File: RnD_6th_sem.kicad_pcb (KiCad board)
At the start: 2 copper layers, 62.1 x 60.5 mm, 63 parts, among them IC1 2EDF7275KXUMA1, J1 HVDC1, J2 PWM, J3 HVDC2, J4 Conn_02x04_Odd_Even, J5 5V, J6 5V, J7 GND2, J8 GND1, J9 Conn_02x04_Odd_Even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

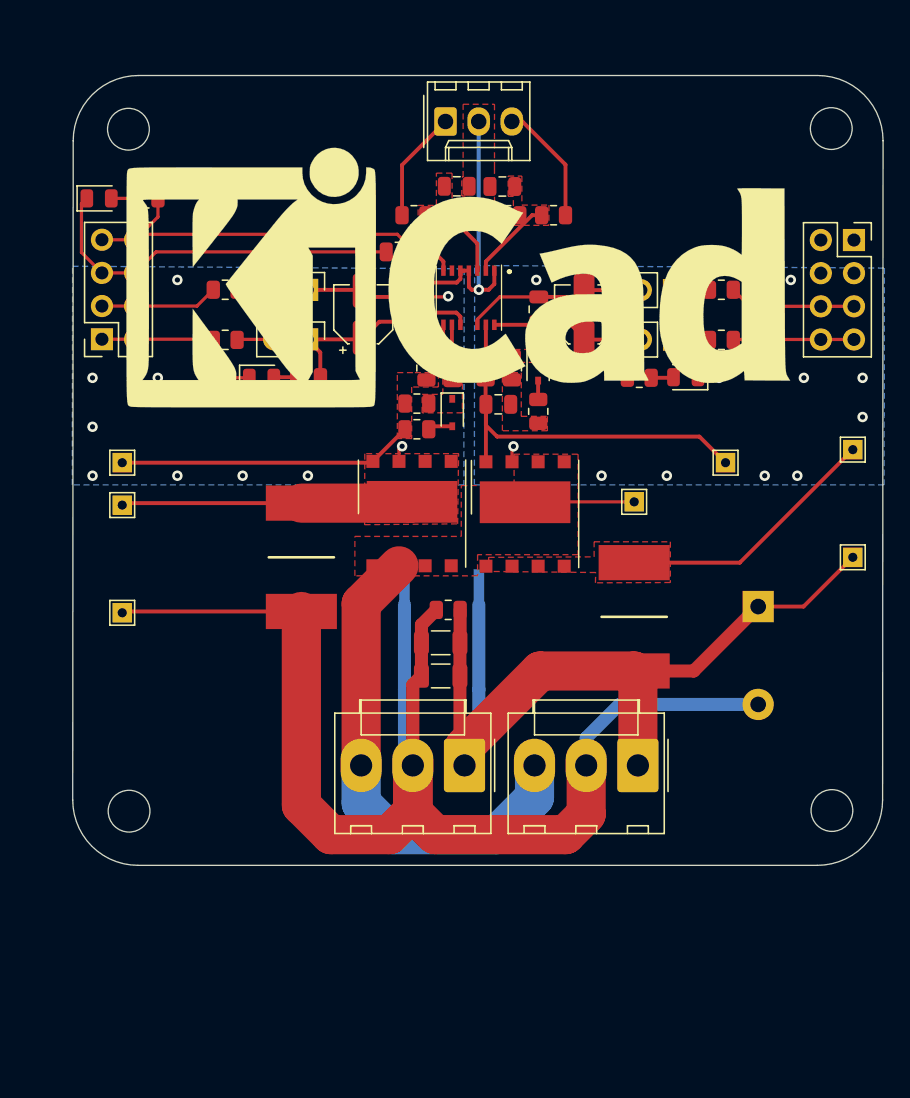
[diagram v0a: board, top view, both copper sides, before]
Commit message: redesigned the power loop
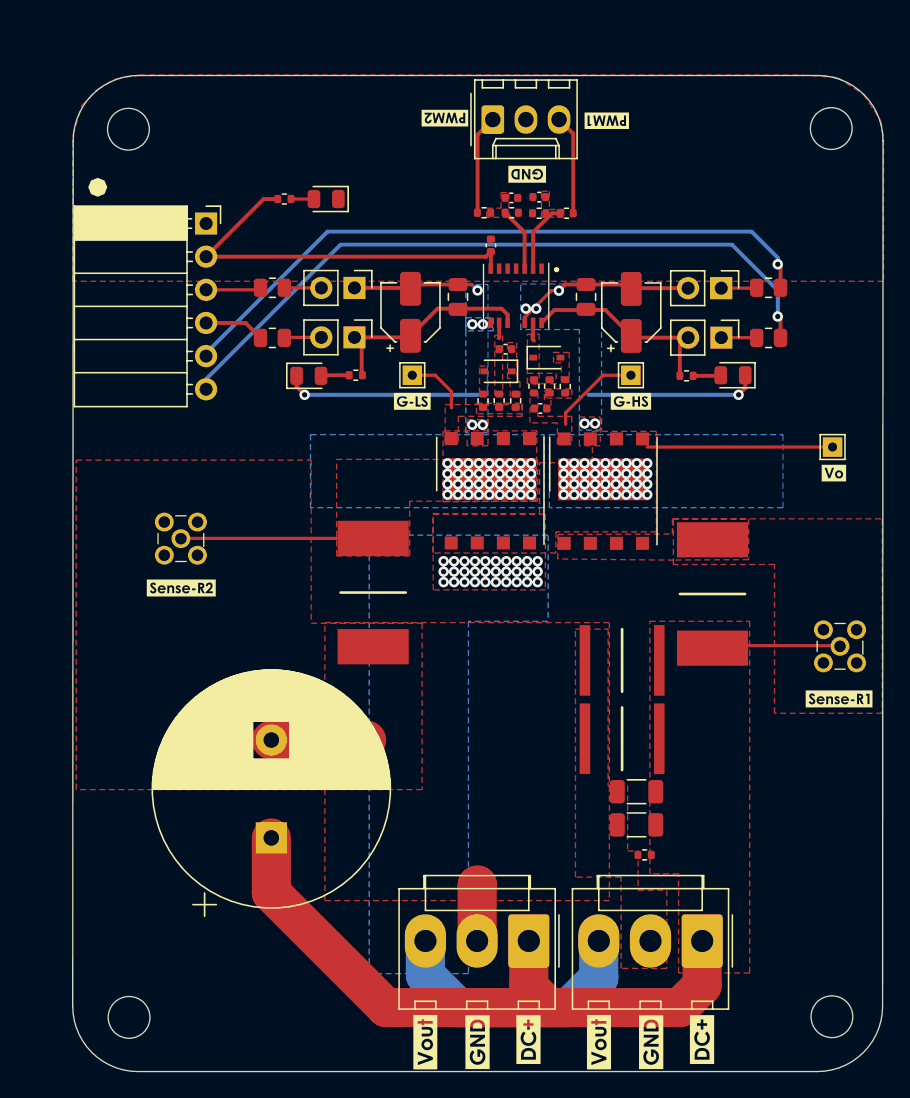
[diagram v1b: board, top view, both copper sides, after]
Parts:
- removed N1: Housing, Symbol:KiCad-Logo_20mm_SilkScreen
- removed TP3, TP5, TP6, TP7: TestPoint_Alt, TestPoint:TestPoint_THTPad_1.5x1.5mm_Drill0.7mm
- added J10: MMCX-J-P-H-ST-TH1, MMCX-J-P-H-ST-TH1:MMCXJPHSTTH1, F.Cu at (112.8, 83.3)
- added kibuzzard-63EDD5C6: G***, kibuzzard-63EDD5C6, F.Cu at (131.8, 74.0)
- added kibuzzard-63EDD5E0: G***, kibuzzard-63EDD5E0, F.Cu at (148.5, 74.0)
- added kibuzzard-63EDD756: G***, kibuzzard-63EDD756, F.Cu at (164.1, 79.5)
- added kibuzzard-63EDD791: G***, kibuzzard-63EDD791, F.Cu at (164.5, 96.8)
- added kibuzzard-63EDD808: G***, kibuzzard-63EDD808, F.Cu at (114.1, 88.3)
- added kibuzzard-63EDD841: G***, kibuzzard-63EDD841, F.Cu at (134.3, 52.3)
- added kibuzzard-63EDD861: G***, kibuzzard-63EDD861, F.Cu at (146.7, 52.5)
- added kibuzzard-63EDD87E: G***, kibuzzard-63EDD87E, F.Cu at (140.6, 56.6)
- added kibuzzard-63EDDA14: G***, kibuzzard-63EDDA14, F.Cu at (107.7, 57.6)
- added kibuzzard-63EE9044: G***, kibuzzard-63EE9044, F.Cu at (154.0, 122.9)
- added kibuzzard-63EE9044: G***, kibuzzard-63EE9044, F.Cu at (140.7, 122.9)
- added kibuzzard-63EE9059: G***, kibuzzard-63EE9059, F.Cu at (150.1, 123.1)
- added kibuzzard-63EE9059: G***, kibuzzard-63EE9059, F.Cu at (136.8, 123.1)
- added kibuzzard-63EE9091: G***, kibuzzard-63EE9091, F.Cu at (132.8, 123.1)
- added kibuzzard-63EE9091: G***, kibuzzard-63EE9091, F.Cu at (146.1, 123.1)
- C1, C13, C14, C4, C5: footprint Capacitor_SMD:C_0805_2012Metric -> Capacitor_SMD:C_0402_1005Metric
- C10, C8, C9: moved to F.Cu
- J4: value Conn_02x04_Odd_Even -> Conn_01x06_Female; footprint Connector_PinSocket_2.54mm:PinSocket_2x04_P2.54mm_Vertical -> Connector_PinSocket_2.54mm:PinSocket_1x06_P2.54mm_Horizontal
- J9: value Conn_02x04_Odd_Even -> MMCX-J-P-H-ST-TH1; footprint Connector_PinSocket_2.54mm:PinSocket_2x04_P2.54mm_Vertical -> MMCX-J-P-H-ST-TH1:MMCXJPHSTTH1
- R1, R10, R11, R12, R13, R14, R15, R16, R2, R3, R4, R5, R6, R8: footprint Resistor_SMD:R_0805_2012Metric -> Resistor_SMD:R_0402_1005Metric
- moved J9 59.6 mm to (163.3, 91.5), turned to 0 degrees
- moved J4 49.7 mm to (116.0, 60.4)
- moved C10 41.3 mm to (121.0, 107.5), turned to 90 degrees
- moved R8 24.1 mm to (149.6, 108.8)
- moved TP2 23.2 mm to (131.8, 72.0)
- moved C6 18.9 mm to (149.0, 103.9)
- moved C7 18.9 mm to (149.0, 106.5)
- moved D5 17.4 mm to (125.2, 58.5), turned to 180 degrees
- moved H1 15.8 mm to (163.9, 121.2)
- moved H2 15.8 mm to (110.1, 121.2)
- moved TP4 15.8 mm to (164.0, 77.5)
- moved C9 14.5 mm to (147.9, 93.9)
- moved C8 14.3 mm to (147.9, 99.9)
- moved J1 14.3 mm to (154.0, 115.4)
- moved J3 14.3 mm to (140.7, 115.4)
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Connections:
- J4 pad 1: unconnected-(J4-Pad1) -> GND
- J4 pad 2: unconnected-(J4-Pad2) -> +3.3V
- J4 pad 3: unconnected-(J4-Pad3) -> Net-(FB2-Pad1)
- J4 pad 4: unconnected-(J4-Pad4) -> Net-(FB3-Pad1)
- J4 pad 6: Net-(FB1-Pad2) -> Net-(FB4-Pad1)
- J9 pad 1: Net-(FB3-Pad1) -> HVDC+
- J9 pad 2: Net-(FB3-Pad1) -> Net-(J9-Pad2)
- J9 pad 3: Net-(FB2-Pad1) -> Net-(J9-Pad2)
- J9 pad 4: Net-(FB2-Pad1) -> Net-(J9-Pad2)
- J9 pad 5: GND -> Net-(J9-Pad2)
- Q1 pad 1: Net-(Q1-Pad1) -> Net-(J9-Pad2)
- Q1 pad 2: Net-(Q1-Pad1) -> Net-(J9-Pad2)
- Q1 pad 3: Net-(Q1-Pad1) -> Net-(J9-Pad2)
- Q1 pad 4: Net-(Q1-Pad1) -> Net-(J9-Pad2)
- R7 pad 1: Net-(Q1-Pad1) -> Net-(J9-Pad2)
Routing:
- net GND3: track 105.9 -> 11.6 mm
- net GND: track 54.4 -> 0.00 mm, vias 1 -> 0
- net Net-(FB4-Pad1): track 9.26 -> 54.0 mm, vias 0 -> 1
- net Net-(FB1-Pad2): track 9.77 -> 51.1 mm, vias 0 -> 1
- net Net-(C5-Pad2): track 27.4 -> 7.07 mm
- net Net-(Q1-Pad1): track 20.3 -> 0.00 mm
- net Net-(Q2-Pad8): track 22.7 -> 4.77 mm
- net gnd-2: track 15.0 -> 26.2 mm, vias 12 -> 6
- net Net-(J1-Pad3): track 45.7 -> 34.9 mm, vias 0 -> 66
- net gnd-1: track 16.7 -> 27.4 mm, vias 12 -> 6
- net HVDC+: track 69.4 -> 60.6 mm
- net Net-(J10-Pad1): track 22.3 -> 14.8 mm, vias 0 -> 36
- net Net-(FB2-Pad1): track 9.05 -> 4.23 mm
- net Net-(FB3-Pad1): track 8.55 -> 4.64 mm
- net Net-(D2-Pad2): track 1.89 -> 0.00 mm
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- added copper zone on F.Cu, net GND3
- added copper zone on F.Cu, net HVDC+
- added copper zone on F.Cu, net Net-(C5-Pad2)
- added copper zone on F.Cu, net Net-(D1-Pad2)
- added copper zone on F.Cu, net Net-(D2-Pad2)
- added copper zone on B.Cu, net Net-(J1-Pad3)
- added copper zone on B.Cu, net Net-(J10-Pad1)
- added copper zone on F.Cu, net Net-(J9-Pad2)
- added copper zone on F.Cu, net gnd-1
- added copper zone on F.Cu, net gnd-2
- removed copper zone on F.Cu, net Net-(Q1-Pad1)
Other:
- board size 62.1 x 60.5 mm -> 62.1 x 76.3 mm
- board text added: "change power loop vias for heat tranfer bottom layer for output right angled connectors for power board 0402 ccomponents connect sense resisots directly to mmcx with test points(research about tt pointys)"
- board text removed: "keep everything closer add common mode choke use smaller track check new power bricks"

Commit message: updated schematic
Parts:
- C1, C13, C14, C4, C5: footprint Capacitor_SMD:C_0402_1005Metric -> Capacitor_SMD:C_0805_2012Metric
- C15, C16: footprint Capacitor_SMD:CP_Elec_4x5.8 -> Capacitor_SMD:CP_Elec_5x5.3
- C8, C9: value 1uF/450V -> 100nF/450V; footprint CGA9P4X7T2W105K250KA:CAPC5750X280N -> Capacitor_SMD:C_1206_3216Metric
- J1: value HVDC1 -> HVDC
- J3: value HVDC2 -> HVDC
- J7: value GND2 -> GND
- J8: value GND1 -> GND
- R1, R10, R11, R12, R13, R14, R15, R16, R2, R3, R4, R5, R6, R8: footprint Resistor_SMD:R_0402_1005Metric -> Resistor_SMD:R_0805_2012Metric
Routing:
- net Net-(C5-Pad2): track 7.07 -> 0.00 mm
- net Net-(C5-Pad1): track 0.00 -> 7.07 mm

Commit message: Updated final design
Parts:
- IC1: footprint 2EDF7275KXUMA1:2EDF7275KXUMA1 -> 2EDF7275K:TFLGA65P500X500X106-14_13N-V
- J4: value Conn_01x06_Female -> Conn_02x05_Odd_Even; footprint Connector_PinSocket_2.54mm:PinSocket_1x06_P2.54mm_Horizontal -> 61201021621:SHDR10W64P254_2X5_2036X885X925P
- moved J4 6.60 mm to (109.4, 61.3), turned to -90 degrees
- moved C6 4.91 mm to (147.9, 99.1)
- moved C7 4.82 mm to (147.9, 101.8)
- moved R8 4.68 mm to (148.5, 104.2)
- moved C14 4.17 mm to (143.1, 54.5)
- moved R14 4.06 mm to (146.6, 56.9)
- moved kibuzzard-63EDD87E 3.99 mm to (141.8, 52.8)
- moved C13 3.92 mm to (139.6, 54.5)
- moved kibuzzard-63EDD841 3.86 mm to (135.4, 48.6)
- moved kibuzzard-63EDD861 3.86 mm to (147.8, 48.8)
- moved J2 3.81 mm to (139.2, 48.8)
- moved R5 3.77 mm to (146.6, 70.7)
- moved R11 3.77 mm to (155.4, 69.3)
- moved D6 3.73 mm to (158.9, 69.3)
- moved TP1 3.68 mm to (152.0, 73.1)
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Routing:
- net Net-(C5-Pad2): track 0.00 -> 10.2 mm
- net Net-(FB1-Pad2): track 51.1 -> 58.9 mm
- net Net-(FB2-Pad1): track 4.23 -> 11.4 mm
- net Net-(C5-Pad1): track 7.07 -> 0.00 mm
- net +3.3V: track 30.6 -> 36.4 mm
- net Net-(FB3-Pad1): track 4.64 -> 9.50 mm
- net gnd-2: track 26.2 -> 30.5 mm
- net gnd-1: track 27.4 -> 31.1 mm
- net Net-(J2-Pad1): track 7.63 -> 9.66 mm
- net Net-(J2-Pad3): track 7.63 -> 9.40 mm
- net Net-(FB4-Pad1): track 54.0 -> 55.6 mm
- net Net-(Q2-Pad8): track 4.77 -> 6.13 mm
- net OUTA: track 1.42 -> 2.66 mm
- net LED2: track 16.6 -> 17.7 mm
- net OUTB: track 1.18 -> 2.02 mm
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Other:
- board size 62.1 x 76.3 mm -> 62.1 x 80 mm
- board text added: "No PWM connector silkscreen review"
- board text removed: "change power loop vias for heat tranfer bottom layer for output right angled connectors for power board 0402 ccomponents connect sense resisots directly to mmcx with test points(research about tt pointys)"

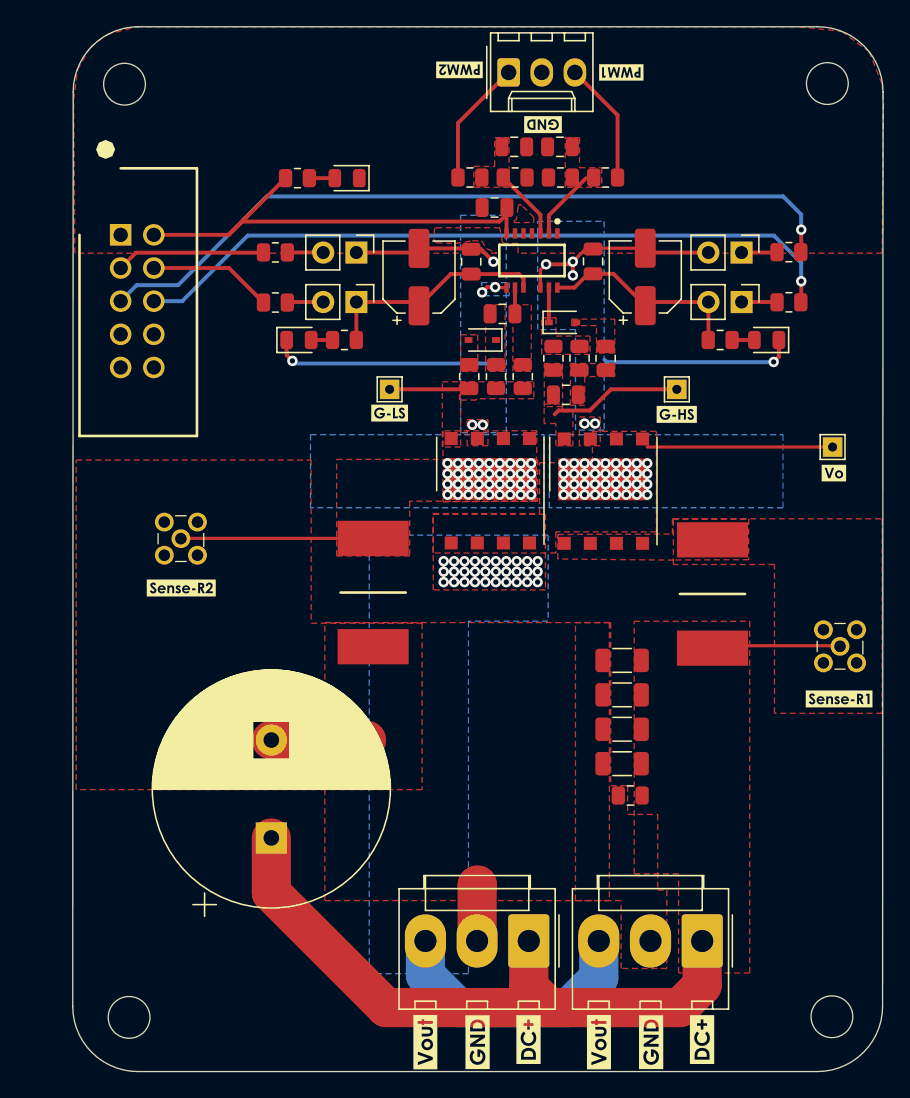
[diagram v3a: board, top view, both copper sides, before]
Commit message: updated design
optimized the size and layout
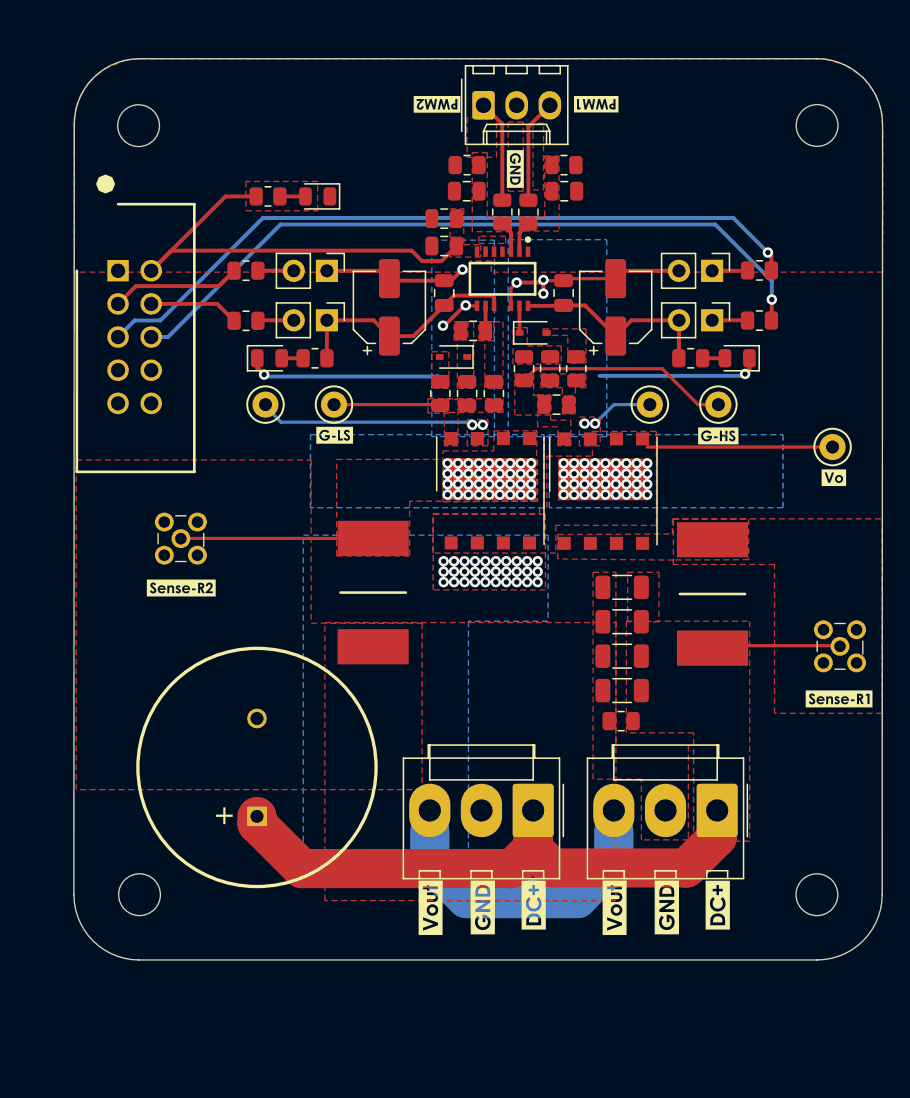
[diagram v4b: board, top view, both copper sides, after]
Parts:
- added C11: 100nF, Capacitor_SMD:C_0805_2012Metric, F.Cu at (134.2, 60.0)
- added TP3: TestPoint_Alt, TestPoint:TestPoint_Keystone_5000-5004_Miniature, F.Cu at (120.5, 74.3)
- added TP5: TestPoint_Alt, TestPoint:TestPoint_Keystone_5000-5004_Miniature, F.Cu at (150.0, 74.3)
- C10: footprint Capacitor_THT:CP_Radial_D18.0mm_P7.50mm -> EKXL451ELL101MM30S:CAPPRD750W80D1825H3200
- TP1, TP2, TP4: footprint TestPoint:TestPoint_THTPad_1.5x1.5mm_Drill0.7mm -> TestPoint:TestPoint_Keystone_5000-5004_Miniature
- moved kibuzzard-63EE9059 10.4 mm to (151.3, 112.8)
- moved kibuzzard-63EE9044 10.4 mm to (155.2, 112.6)
- moved kibuzzard-63EE9091 10.4 mm to (147.3, 112.8)
- moved kibuzzard-63EE9059 10.3 mm to (137.2, 112.8)
- moved kibuzzard-63EE9044 10.3 mm to (141.1, 112.6)
- moved kibuzzard-63EE9091 10.3 mm to (133.2, 112.8)
- moved J1 10.1 mm to (155.1, 105.4)
- moved J3 10.0 mm to (141.0, 105.4)
- moved H2 9.43 mm to (110.9, 111.8)
- moved H1 9.42 mm to (162.8, 111.8)
- moved R14 6.48 mm to (140.7, 59.5), turned to -90 degrees
- moved R8 5.74 mm to (147.8, 98.5)
- moved C6 5.60 mm to (147.9, 93.5)
- moved C8 5.60 mm to (147.9, 90.9)
- moved C7 5.60 mm to (147.9, 96.2)
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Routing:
- net gnd-2: track 30.5 -> 45.6 mm
- net GND3: track 11.6 -> 0.00 mm
- net Net-(C5-Pad2): track 10.2 -> 16.4 mm
- net HVDC+: track 60.6 -> 57.2 mm
- net PWM2: track 5.47 -> 2.40 mm
- net PWM1: track 5.41 -> 2.41 mm
- net Net-(FB1-Pad2): track 58.9 -> 56.1 mm
- net Net-(FB3-Pad1): track 9.50 -> 6.89 mm
- net gnd-1: track 31.1 -> 33.4 mm
- net Net-(Q2-Pad8): track 6.13 -> 8.18 mm
- net Net-(J2-Pad1): track 9.66 -> 7.86 mm
- net Net-(FB2-Pad1): track 11.4 -> 9.94 mm
- net Net-(J2-Pad3): track 9.40 -> 7.95 mm
- net +3.3V: track 36.4 -> 35.2 mm
- net OUTA: track 2.66 -> 2.07 mm
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- added copper zone on F.Cu, net +3.3V
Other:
- board size 62.1 x 80 mm -> 62 x 69.1 mm
- board text added: "+"
- board text added: "0.8mm test points k-s test points move the connects and caps up"
- board text removed: "No PWM connector silkscreen review"

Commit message: updated silkscreen
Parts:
- removed kibuzzard-63EDD808: G***, kibuzzard-63EDD808
- removed kibuzzard-63EDD841: G***, kibuzzard-63EDD841
- removed kibuzzard-63EDD861: G***, kibuzzard-63EDD861
- removed kibuzzard-63EDD87E: G***, kibuzzard-63EDD87E
- added kibuzzard-63FF19DB: G***, kibuzzard-63FF19DB, F.Cu at (139.7, 56.1)
- added kibuzzard-63FF19FC: G***, kibuzzard-63FF19FC, F.Cu at (145.7, 51.3)
- added kibuzzard-63FF1A06: G***, kibuzzard-63FF1A06, F.Cu at (133.5, 51.3)
- added kibuzzard-63FF1A39: G***, kibuzzard-63FF1A39, F.Cu at (114.1, 88.3)
- added kibuzzard-63FF1AED: G***, kibuzzard-63FF1AED, F.Cu at (118.0, 74.3)
- added kibuzzard-63FF1AF8: G***, kibuzzard-63FF1AF8, F.Cu at (147.3, 74.3)
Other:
- board text removed: "0.8mm test points k-s test points move the connects and caps up"
